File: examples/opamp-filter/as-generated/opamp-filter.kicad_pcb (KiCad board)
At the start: 2 copper layers, 58 x 42 mm, 22 parts, among them J1 IN, J2 5V, J3 OUT, U1 MCP6001R, U2 MCP6001R

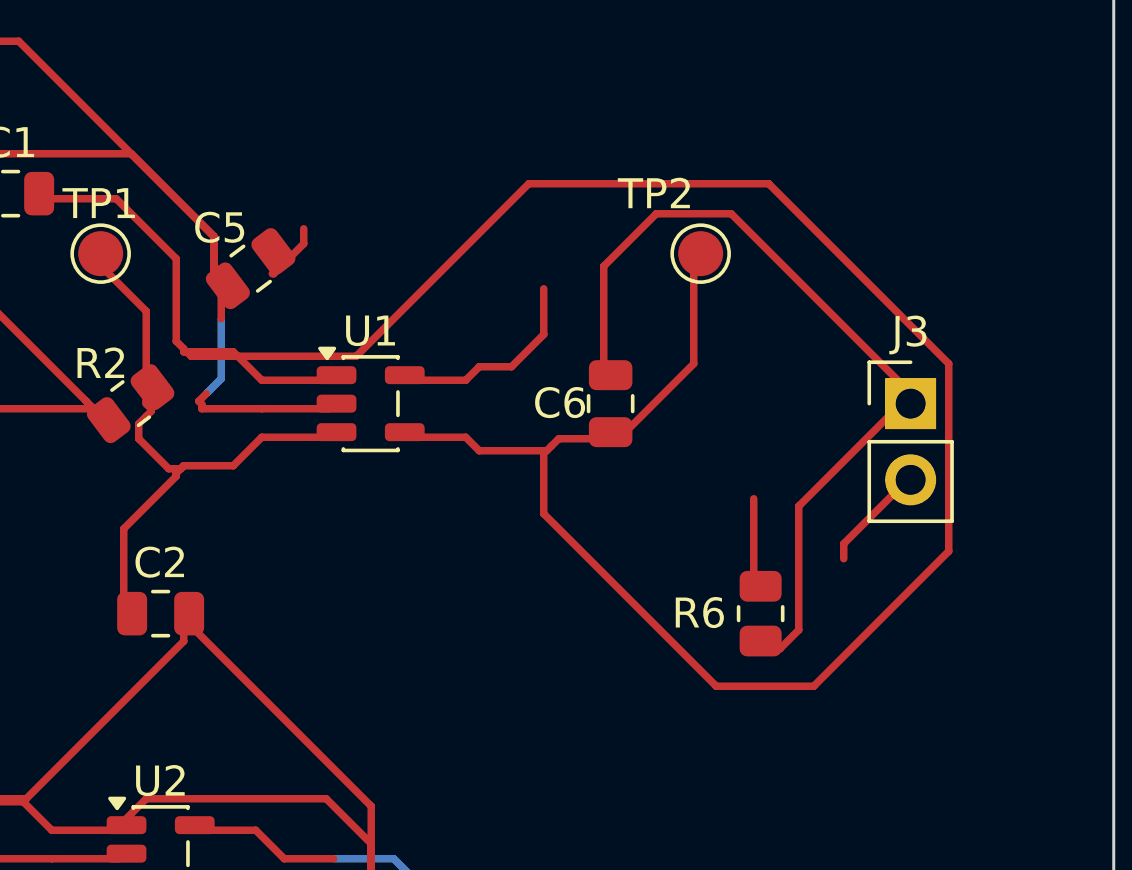
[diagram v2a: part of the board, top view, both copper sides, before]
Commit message: Rip up copper that tours, and put a footprint's zones where the footprint is
The plots showed three things on the artwork side that no rule reported.

**A track that goes round the board to cover thirteen millimetres.** The
op-amp's feedback wrap had to get from one side of a SOT-23-5 to the other
and, routed last, took fifty-six millimetres of tour because everything
nearer was already spoken for. That is an ordering problem, so the loop that
fixes ordering fixes it: `_route_all` now reports what each track cost
against `route.wander`'s own baseline - imported, not copied, so the two
cannot drift - and the worst tour goes to the front and the set is routed
again. A track that still tours from first pick has nowhere better to be and
is left alone. The default order is shortest-first for the same reason: a
thirteen millimetre connection has few ways to be made and a forty
millimetre one has many. The learned order is now written on every change,
not only on success, because an afternoon of rip-ups is worth keeping when
the machine goes away in the middle.

**A keep-out sitting at the origin.** A footprint may carry zones of its own
and KiCad stores *those* in board coordinates while everything else in a
footprint is stored relative to it. The Pico module's two pad keep-outs had
been at (0, -6) for four rounds - off the board, keeping nothing out. DRC is
silent because an empty region violates no rule, and the only visible sign
was the plot: "fit to page" fits the bounding box, so every view of that
board came out at half scale in one corner with the rest blank.
`layout.zone_outside_outline` reports it; the placer moves it.

**Silkscreen printed through silkscreen.** The schematic has
`readability.text_over_text` and the board had nothing, though the board is
the harder case - a sheet can be zoomed and a bare board cannot.
`silk.text_over_text` measures it from the font size the file states; on
KiCad's demo boards it fires on 6 of 16, 173 times. The generator places t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
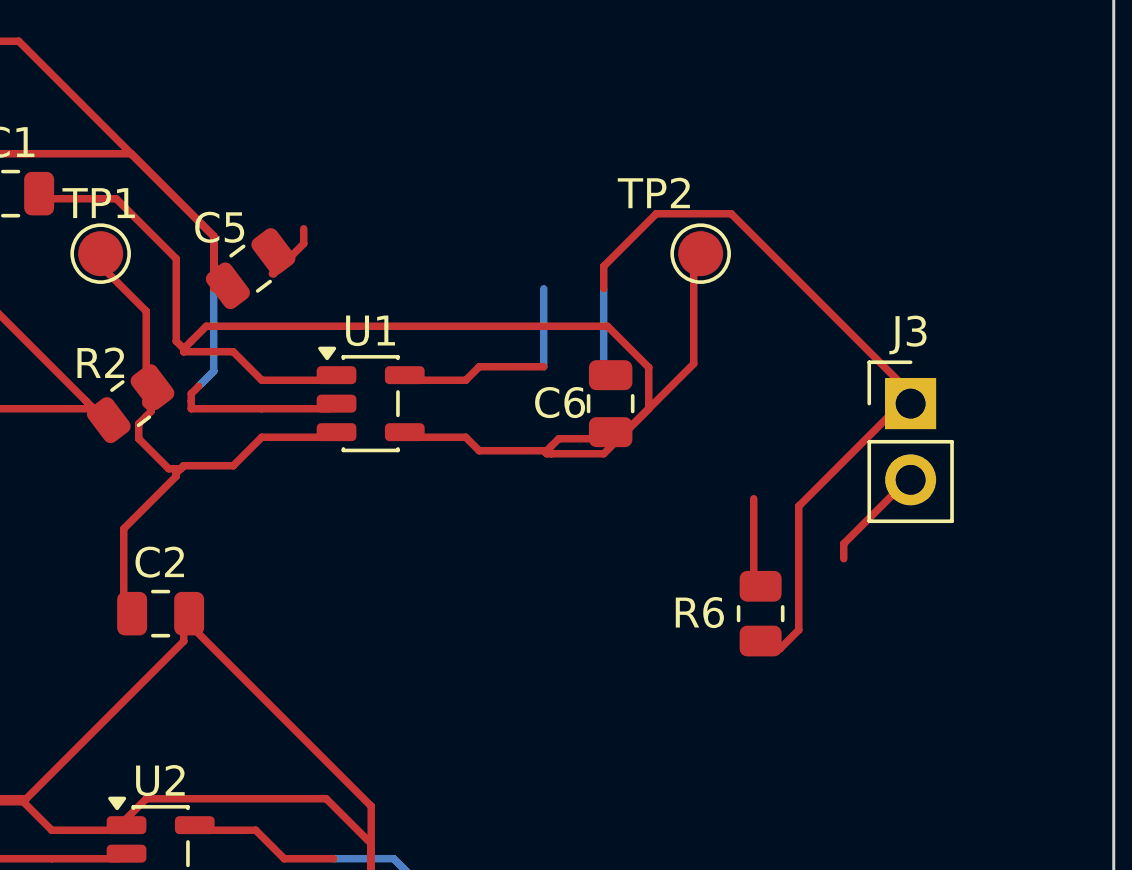
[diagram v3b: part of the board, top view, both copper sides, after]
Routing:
- net /OUT: track 85.4 -> 50.9 mm
- net GND: track 53.8 -> 54.5 mm
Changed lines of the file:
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@@
 	(segment (start 128.65 75.1) (end 127.0 75.1) (width 0.25) (layer "F.Cu") (net 7))
 	(segment (start 131.8625 77.0) (end 129.6 77.0) (width 0.25) (layer "F.Cu") (net 2))
-	(segment (start 129.6 77.0) (end 127.604 77.0) (width 0.25) (layer "F.Cu") (net 2))
-	(segment (start 127.604 77.0) (end 127.604 76.854) (width 0.25) (layer "F.Cu") (net 2))
-	(segment (start 127.604 76.854) (end 127.5 76.75) (width 0.25) (layer "F.Cu") (net 2))
-	(segment (start 127.5 76.75) (end 127.75 76.5) (width 0.25) (layer "F.Cu") (net 2))
+	(segment (start 129.6 77.0) (end 127.25 77.0) (width 0.25) (layer "F.Cu") (net 2))
+	(segment (start 127.25 77.0) (end 127.25 76.75) (width 0.25) (layer "F.Cu") (net 2))
+	(segment (start 127.25 76.75) (end 127.25 76.5) (width 0.25) (layer "F.Cu") (net 2))
+	(segment (start 127.25 76.5) (end 127.5 76.25) (width 0.25) (layer "F.Cu") (net 2))
 	(segment (start 131.8625 77.95) (end 129.6 77.95) (width 0.25) (layer "F.Cu") (net 3))
 	(segment (start 129.6 77.95) (end 128.65 78.9) (width 0.25) (layer "F.Cu") (net 3))
@@
 	(segment (start 134.1375 76.05) (end 136.4 76.05) (width 0.25) (layer "F.Cu") (net 1))
 	(segment (start 136.4 76.05) (end 136.85 75.6) (width 0.25) (layer "F.Cu") (net 1))
-	(segment (start 136.85 75.6) (end 137.925 75.6) (width 0.25) (layer "F.Cu") (net 1))
-	(segment (start 137.925 75.6) (end 139.0 74.525) (width 0.25) (layer "F.Cu") (net 1))
-	(segment (start 139.0 74.525) (end 139.0 73.0) (width 0.25) (layer "F.Cu") (net 1))
+	(segment (start 136.85 75.6) (end 139.0 75.6) (width 0.25) (layer "F.Cu") (net 1))
 	(segment (start 134.1375 77.95) (end 136.4 77.95) (width 0.25) (layer "F.Cu") (net 7))
 	(segment (start 136.4 77.95) (end 136.85 78.4) (width 0.25) (layer "F.Cu") (net 7))
@@
 	(segment (start 126.75 79.25) (end 126.75 79.15) (width 0.25) (layer "F.Cu") (net 3))
 	(segment (start 126.75 79.15) (end 127.0 78.9) (width 0.25) (layer "F.Cu") (net 3))
-	(segment (start 127.0 75.1) (end 127.1 75.1) (width 0.25) (layer "F.Cu") (net 7))
-	(segment (start 127.1 75.1) (end 127.25 75.25) (width 0.25) (layer "F.Cu") (net 7))
-	(segment (start 127.25 75.25) (end 132.75 75.25) (width 0.25) (layer "F.Cu") (net 7))
-	(segment (start 132.75 75.25) (end 138.5 69.5) (width 0.25) (layer "F.Cu") (net 7))
-	(segment (start 138.5 69.5) (end 146.5 69.5) (width 0.25) (layer "F.Cu") (net 7))
-	(segment (start 146.5 69.5) (end 152.5 75.5) (width 0.25) (layer "F.Cu") (net 7))
-	(segment (start 152.5 75.5) (end 152.5 81.75) (width 0.25) (layer "F.Cu") (net 7))
-	(segment (start 152.5 81.75) (end 148.0 86.25) (width 0.25) (layer "F.Cu") (net 7))
-	(segment (start 148.0 86.25) (end 144.75 86.25) (width 0.25) (layer "F.Cu") (net 7))
-	(segment (start 144.75 86.25) (end 139.0 80.5) (width 0.25) (layer "F.Cu") (net 7))
-	(segment (start 139.0 80.5) (end 139.0 78.4) (width 0.25) (layer "F.Cu") (net 7))
+	(segment (start 127.0 75.1) (end 127.0 75.0) (width 0.25) (layer "F.Cu") (net 7))
+	(segment (start 127.0 75.0) (end 127.25 74.75) (width 0.25) (layer "F.Cu") (net 7))
+	(segment (start 127.25 74.75) (end 127.75 74.25) (width 0.25) (layer "F.Cu") (net 7))
+	(segment (start 127.75 74.25) (end 141.125 74.25) (width 0.25) (layer "F.Cu") (net 7))
+	(segment (start 141.125 74.25) (end 142.5 75.625) (width 0.25) (layer "F.Cu") (net 7))
+	(segment (start 142.5 75.625) (end 142.5 77.0) (width 0.25) (layer "F.Cu") (net 7))
+	(segment (start 142.5 77.0) (end 141.0 78.5) (width 0.25) (layer "F.Cu") (net 7))
+	(segment (start 141.0 78.5) (end 139.25 78.5) (width 0.25) (layer "F.Cu") (net 7))
+	(segment (start 139.25 78.5) (end 139.1 78.5) (width 0.25) (layer "F.Cu") (net 7))
+	(segment (start 139.1 78.5) (end 139.0 78.4) (width 0.25) (layer "F.Cu") (net 7))
 	(segment (start 127.0 75.1) (end 127.0 75.0) (width 0.25) (layer "F.Cu") (net 7))
 	(segment (start 127.0 75.0) (end 126.75 74.75) (width 0.25) (layer "F.Cu") (net 7))
@@
 	(segment (start 126.75 72.0) (end 124.75 70.0) (width 0.25) (layer "F.Cu") (net 7))
 	(segment (start 124.75 70.0) (end 121.95 70.0) (width 0.25) (layer "F.Cu") (net 7))
-	(segment (start 141.0 76.05) (end 141.0 72.25) (width 0.25) (layer "F.Cu") (net 8))
+	(segment (start 141.0 76.05) (end 141.0 75.5) (width 0.25) (layer "F.Cu") (net 8))
+	(segment (start 141.0 75.5) (end 141.0 73.0) (width 0.25) (layer "B.Cu") (net 8))
+	(segment (start 141.0 73.0) (end 141.0 72.25) (width 0.25) (layer "F.Cu") (net 8))
 	(segment (start 141.0 72.25) (end 142.75 70.5) (width 0.25) (layer "F.Cu") (net 8))
 	(segment (start 142.75 70.5) (end 145.25 70.5) (width 0.25) (layer "F.Cu") (net 8))
@@
 	(segment (start 128.0 72.25) (end 128.0 72.45) (width 0.25) (layer "F.Cu") (net 2))
 	(segment (start 128.0 72.45) (end 128.05 72.5) (width 0.25) (layer "F.Cu") (net 2))
-	(segment (start 128.05 72.5) (end 128.05 72.55) (width 0.25) (layer "F.Cu") (net 2))
-	(segment (start 128.05 72.55) (end 128.25 72.75) (width 0.25) (layer "F.Cu") (net 2))
-	(segment (start 128.25 72.75) (end 128.25 74.0) (width 0.25) (layer "F.Cu") (net 2))
-	(segment (start 128.25 74.0) (end 128.25 76.0) (width 0.25) (layer "B.Cu") (net 2))
-	(segment (start 128.25 76.0) (end 127.75 76.5) (width 0.25) (layer "B.Cu") (net 2))
+	(segment (start 128.05 72.5) (end 128.05 72.7) (width 0.25) (layer "F.Cu") (net 2))
+	(segment (start 128.05 72.7) (end 128.0 72.75) (width 0.25) (layer "F.Cu") (net 2))
+	(segment (start 128.0 72.75) (end 128.0 73.0) (width 0.25) (layer "F.Cu") (net 2))
+	(segment (start 128.0 73.0) (end 128.0 75.75) (width 0.25) (layer "B.Cu") (net 2))
+	(segment (start 128.0 75.75) (end 127.5 76.25) (width 0.25) (layer "B.Cu") (net 2))
 	(segment (start 128.05 72.5) (end 128.05 72.3) (width 0.25) (layer "F.Cu") (net 2))
 	(segment (start 128.05 72.3) (end 128.0 72.25) (width 0.25) (layer "F.Cu") (net 2))
@@
 	(segment (start 107.75 95.0) (end 108.0 95.0) (width 0.25) (layer "B.Cu") (net 1))
 	(segment (start 108.0 95.0) (end 111.0 98.0) (width 0.25) (layer "B.Cu") (net 1))
+	(segment (start 139.0 75.6) (end 139.0 73.0) (width 0.25) (layer "B.Cu") (net 1))
 	(segment (start 132.0 92.0) (end 134.0 92.0) (width 0.25) (layer "B.Cu") (net 1))
 	(segment (start 134.0 92.0) (end 136.0 94.0) (width 0.25) (layer "B.Cu") (net 1))

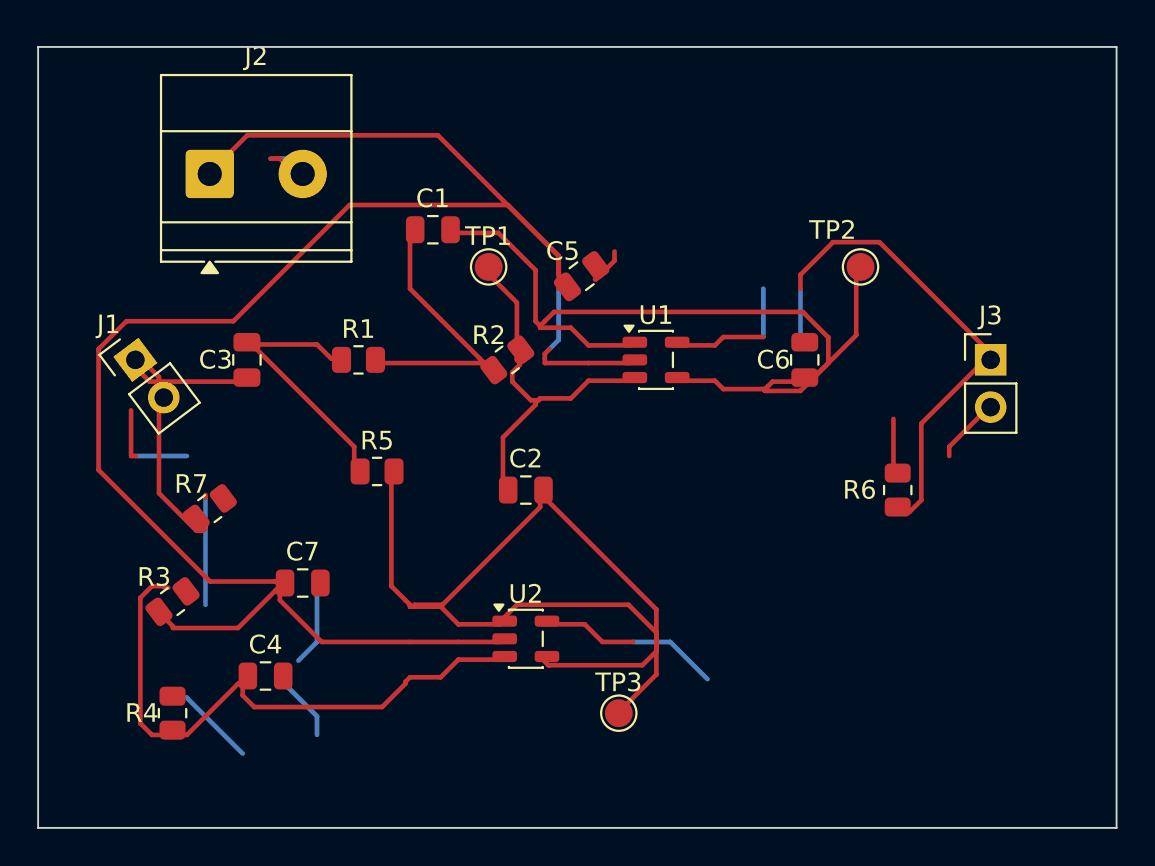
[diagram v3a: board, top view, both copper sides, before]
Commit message: Learn the drawing from the boards people drew
The brief for this round: relying on the autorouter and the numbers alone is
not enough - organise what pictorial correctness looks like from ordinary
circuits and open designs, and improve the drawing itself. So it starts in
KiCad's own demo corpus, measured and looked at, and ends with the habits
pushed into the generator.

tools/board_signature.py (new) reduces "looks autorouted" to five numbers.
Hand-routed two-layer boards cluster tightly: 10-47% of copper on the second
face, median segments 1.8-3.5 mm, 9-25 corners per decimetre, 91-98% of them
45s, 0.3-16 vias per decimetre. Rendering interf_u beside our boards says the
same thing in one glance: a layer has a direction, a bus travels as a bundle,
a person covers an offset with the long straight and one diagonal.

Three habits, now in the generator:

* Router.route(follow=...): cells beside a sibling net's path are discounted,
  so a bus (nets sharing a name prefix - I2S_*, SPI_*) travels as parallel
  lanes in one corridor. The discount is a fraction of a step, so it never
  buys a detour.
* _doglegged: every wiggly stretch is redrawn as the human stroke - the
  straight along the dominant direction plus one 45 - when the dogleg is
  clear, recursing into halves where a crossing blocks the whole. The op-amp
  board's median segment rose from 0.75 mm and its corner rate fell from
  38/dm; the FPGA board landed at 1.54 mm and 17.8/dm, inside the human band.
* Purposeful stitching: the 6 mm via carpet is gone. A ring at the rim, vias
  beside every back-layer crossing (where the plane is actually cut), and a
  coarse 12 mm mesh so no pour orphans. Vias/dm: buck 41 -> 18, carrier
  28 -> 13, all five inside the corpus band, pour_fragmented still silent.

Three failures the round produced and what they taught:

* pinned(): reshaping may not move copper off any point inside an own-net
  pad - the centre alone was not enough, a routed run touches off-centre and
  the ove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
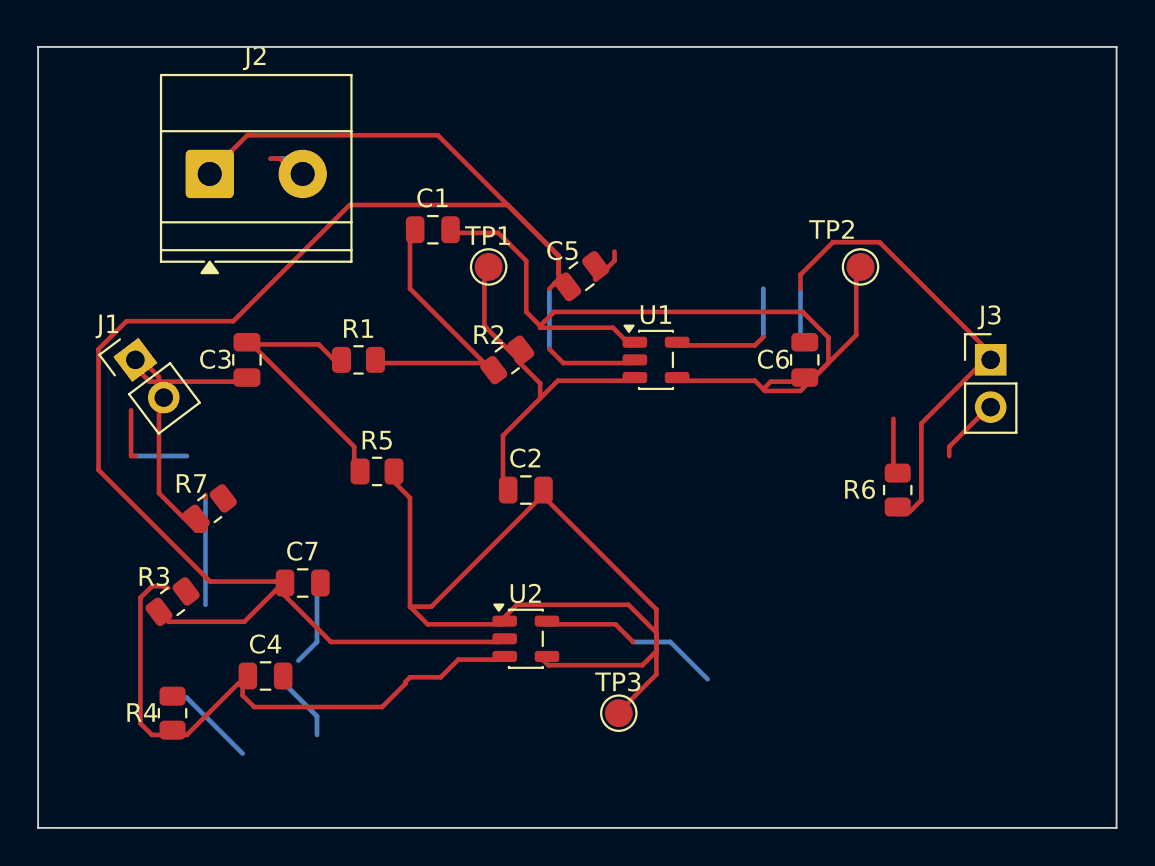
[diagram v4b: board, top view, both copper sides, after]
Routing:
- net +5V: track 103.3 -> 101.9 mm
- net /FILT_IN: track 20.1 -> 19.3 mm

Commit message: A net may not cross its own copper
The reviewer looked at the plots, saw tracks driven through each other, and
asked whether the other checks were really passing. Both halves of the
answer were worth keeping. Measured directly - every pair of same-layer
segments on every reviewed board - there is not one crossing between
different nets: DRC reports zero errors, zero shorts, zero unconnected, and
it is not being fooled. What the plots show is a net crossing *itself*:
thirteen places on the FPGA board, one each on the op-amp and the buck.
Same potential, so DRC has nothing to say; no length ratio catches it; no
rule of ours looked. The checks were honest. The check list had a hole
exactly the shape of what the eye catches first.

route.self_crossing (new, warning, promoted by ai-generated) measures it:
two branches of one net crossing means the copper carries a redundant loop,
and a person never draws one. KiCad's demo corpus: 6 of 16 boards carry one
to three, at dense escapes.

_unlooped (new pass) is the fix, as a graph question: split every same-net
crossing so the X is a node, and while any cycle remains in the net's
copper, remove the longest junction-to-junction chain of the cycle -
connectivity is kept by definition, a cycle has two ways round, and the
amputated X becomes an ordinary corner. The clearance oracle now also
refuses to let _doglegged or _straighten draw a new X over their own net.

The cutter was wrong twice before it was right, both times the same lesson:
KiCad's connectivity is geometric, a track graph is endpoint topology, and
the difference is exactly a pad. The escape fan draws a micro-hook inside
an off-grid pad - the overlap is the connection - and the graph read it as
a dangling loop and amputated the pad's only feed. Nodes inside an own-net
pad are anchors now, a cycle wholly inside one pad is immune, and segments
passing over a pad are split so the feed is a node the cut must respect.

Self-crossings on the five reviewed boards: 0/0/0/0/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
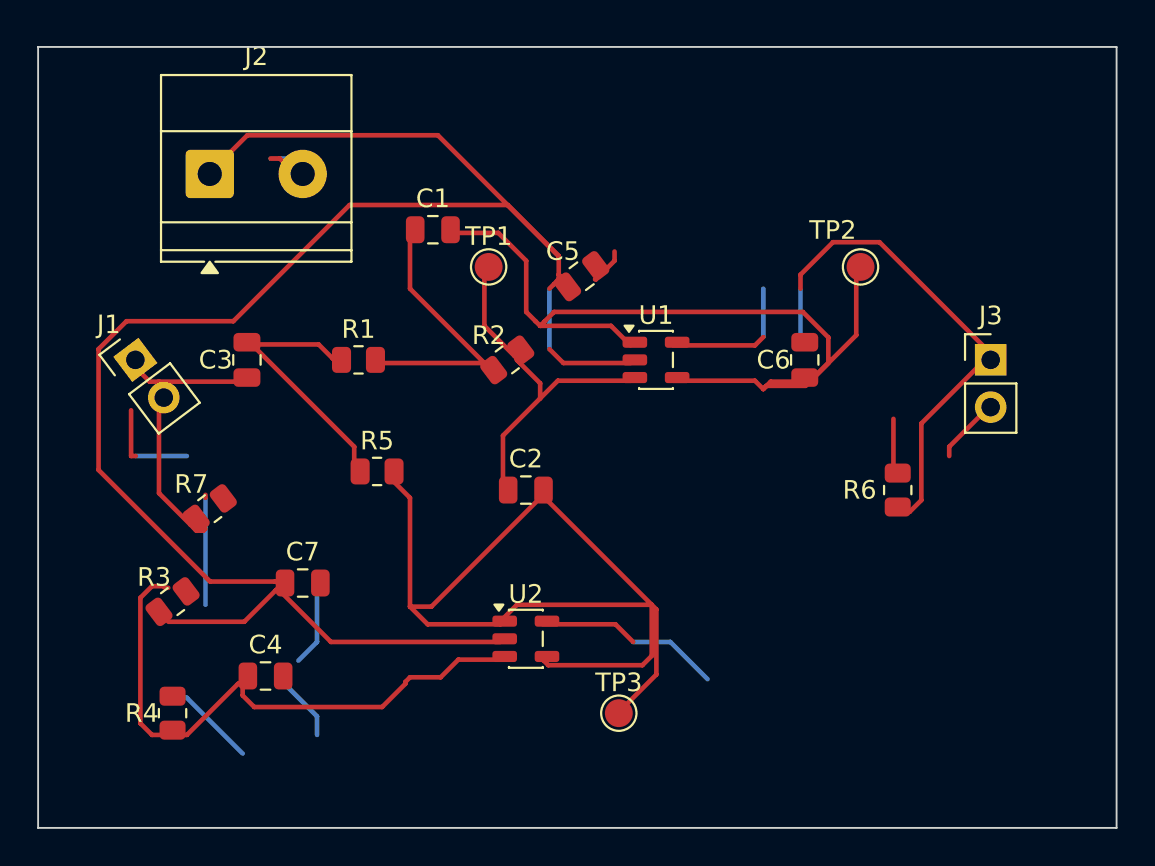
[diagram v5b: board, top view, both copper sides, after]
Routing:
- net /IN: track 17.4 -> 15.8 mm
- net +5V: track 101.9 -> 100.9 mm
- net /VREF: track 55.1 -> 55.6 mm
